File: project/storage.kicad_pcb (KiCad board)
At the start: 6 copper layers, 190 x 134 mm, 60 parts

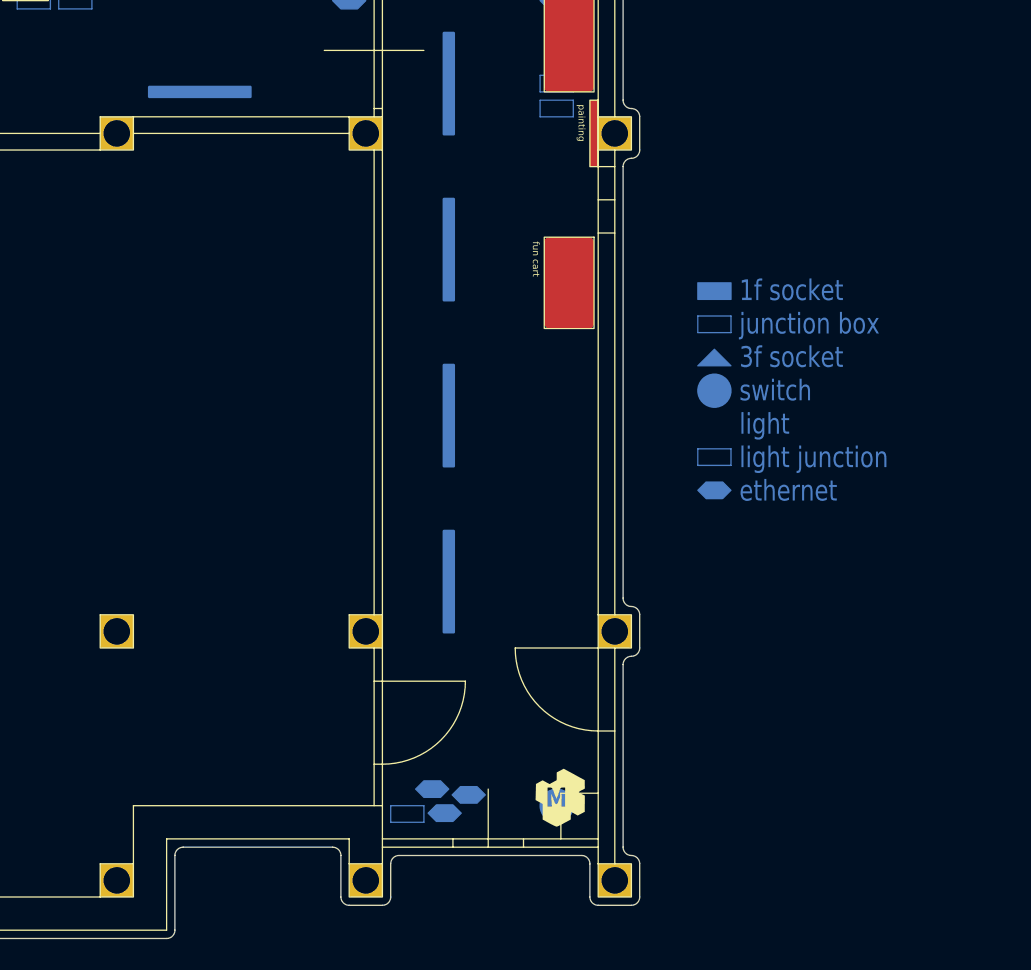
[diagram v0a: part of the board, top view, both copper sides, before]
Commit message: extra comms and power towards hallway
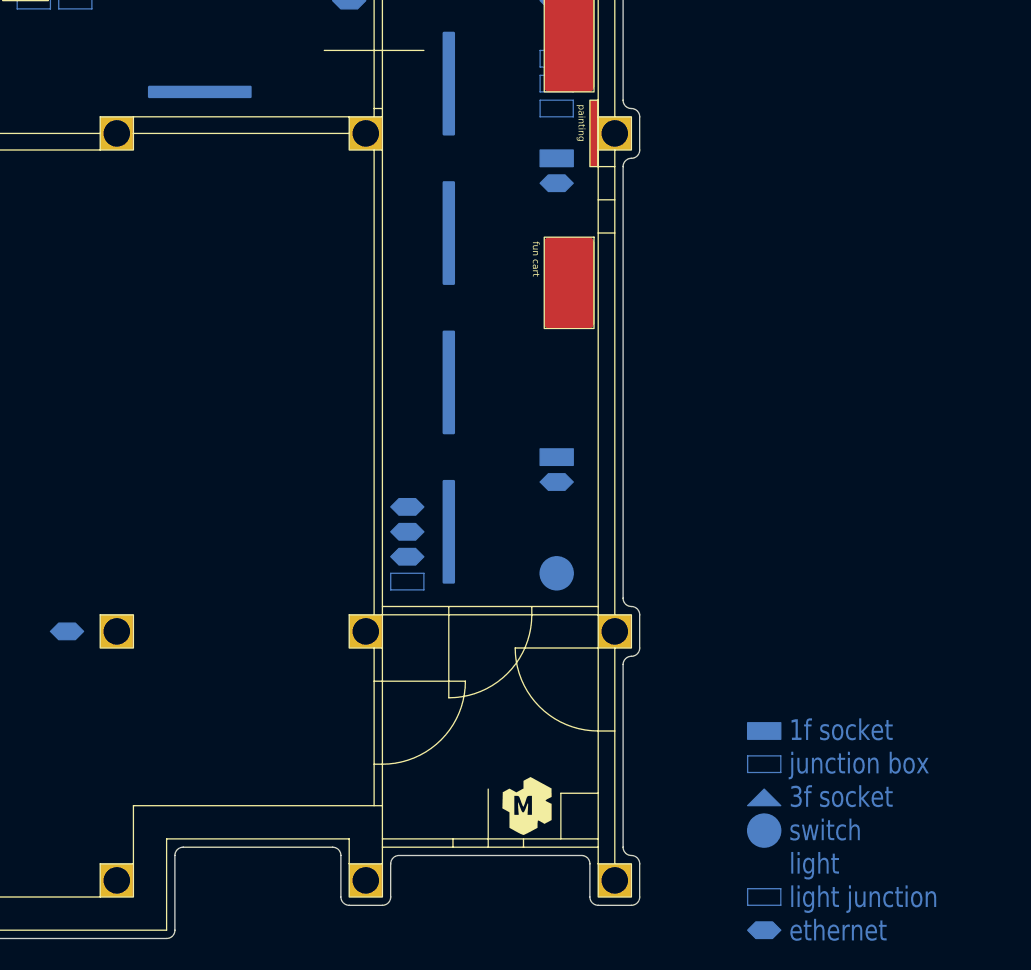
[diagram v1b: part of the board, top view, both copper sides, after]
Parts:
- moved L31 6.00 mm to (217.0, 111.0)
- moved G1 4.12 mm to (226.0, 144.0)
- moved L30 4.00 mm to (217.0, 93.0)
- moved L26 2.00 mm to (217.0, 75.0)
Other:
- board text added: "19"
- board text added: "213"
- board text added: "214"
- board text added: "31"
- board text added: "324"
- board text added: "3x1 10m via P621 sens x1"
- board text added: "3x2.5 2m via D621 x3"
- board text added: "3x2.5 6m via D621 x3"
- board text added: "3x2.5 C16 27m"
- board text added: "7x0.75 B2 23m"
- board text added: "D611"
- board text added: "D612"
- board text added: "D621"
- board text added: "ap-L6 35m"
- board text added: "cam-gate 35m"
- board text added: "hl-G1 28m"
- board text added: "hl-G2 32m"
- board text added: "maglock 35m"
- board text added: "void 42m"
- board text removed: "3x1 13m via P621 sens x1"
- board text removed: "ap-L6 38m"
- board text removed: "cam-gate 38m"
- board text removed: "maglock 38m"
